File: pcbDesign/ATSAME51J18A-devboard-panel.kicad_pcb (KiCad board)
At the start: 2 copper layers, 100 x 100 mm, 300 parts, among them J1 Micro_SD_Card, J10 CAN, J2 BAT, J3 QWIIC, J4 L_PINS, J5 NP_OUT, J6 USB, J7 QSPI, J8 R_PINS, J9 USB4105_REVA, U1 TCAN1051GVDRQ1, U2 ATSAME51J18A-A, U3 MIC5219-5.0YMM, U4 LM27762, U5 LM2775QDSGTQ1, U6 SC630AULTRT, U7 BQ24074RGT, U8 BQ27441DRZR-G1B, Y1 32.768

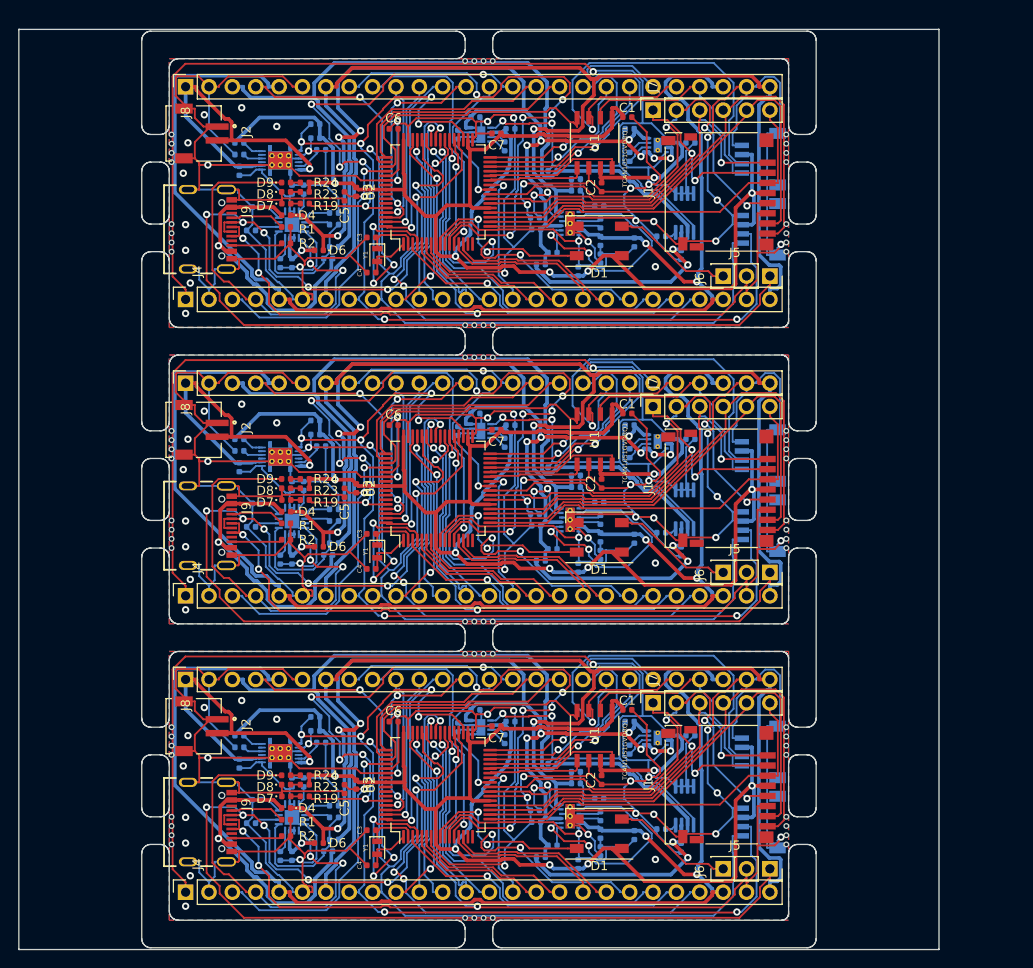
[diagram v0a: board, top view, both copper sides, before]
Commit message: Repanelized board after adding pin descriptions
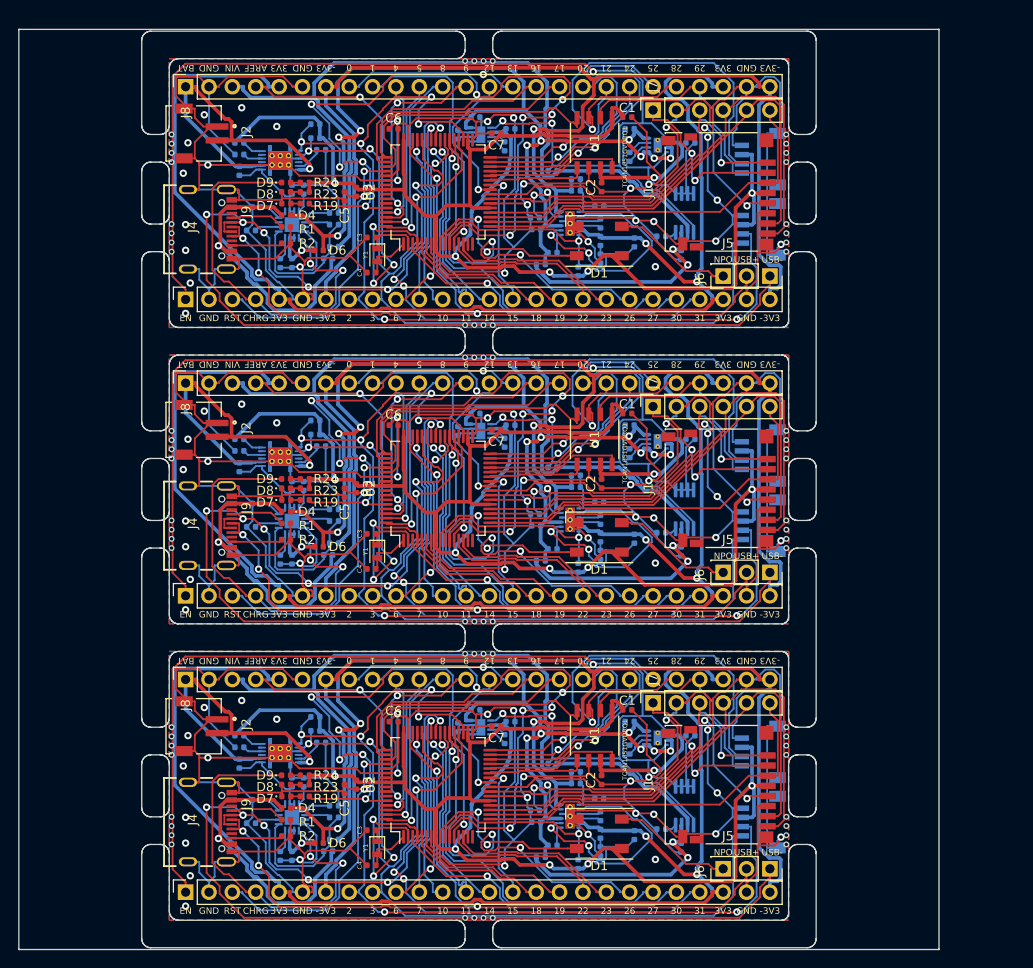
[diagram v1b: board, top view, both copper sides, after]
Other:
- board text added: "-3V3"
- board text added: "-3v3"
- board text added: "0"
- board text added: "1"
- board text added: "10"
- board text added: "11"
- board text added: "12"
- board text added: "13"
- board text added: "14"
- board text added: "15"
- board text added: "16"
- board text added: "17"
- board text added: "18"
- board text added: "19"
- board text added: "2"
- board text added: "20"
- board text added: "21"
- board text added: "22"
- board text added: "23"
- board text added: "24"
- board text added: "25"
- board text added: "26"
- board text added: "27"
- board text added: "28"
- board text added: "29"
- board text added: "3"
- board text added: "30"
- board text added: "31"
- board text added: "3V3"
- board text added: "4"
- board text added: "5"
- board text added: "6"
- board text added: "7"
- board text added: "8"
- board text added: "9"
- board text added: "AREF"
- board text added: "BAT"
- board text added: "CANH"
- board text added: "CANL"
- board text added: "CHRG"
- board text added: "CS"
- board text added: "EN"
- board text added: "GND"
- board text added: "I2SDI"
- board text added: "I2SDO"
- board text added: "I2SMCLK"
- board text added: "I2SSCK"
- board text added: "I2SWS"
- board text added: "MI"
- board text added: "MO"
- board text added: "NPO"
- board text added: "QCS"
- board text added: "QD0"
- board text added: "QD1"
- board text added: "QD2"
- board text added: "QD3"
- board text added: "QSCK"
- board text added: "RST"
- board text added: "RX"
- board text added: "SCK"
- board text added: "SCL"
- board text added: "SDA"
- board text added: "TX"
- board text added: "USB+"
- board text added: "USB-"
- board text added: "VIN"

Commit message: Panelized the final design
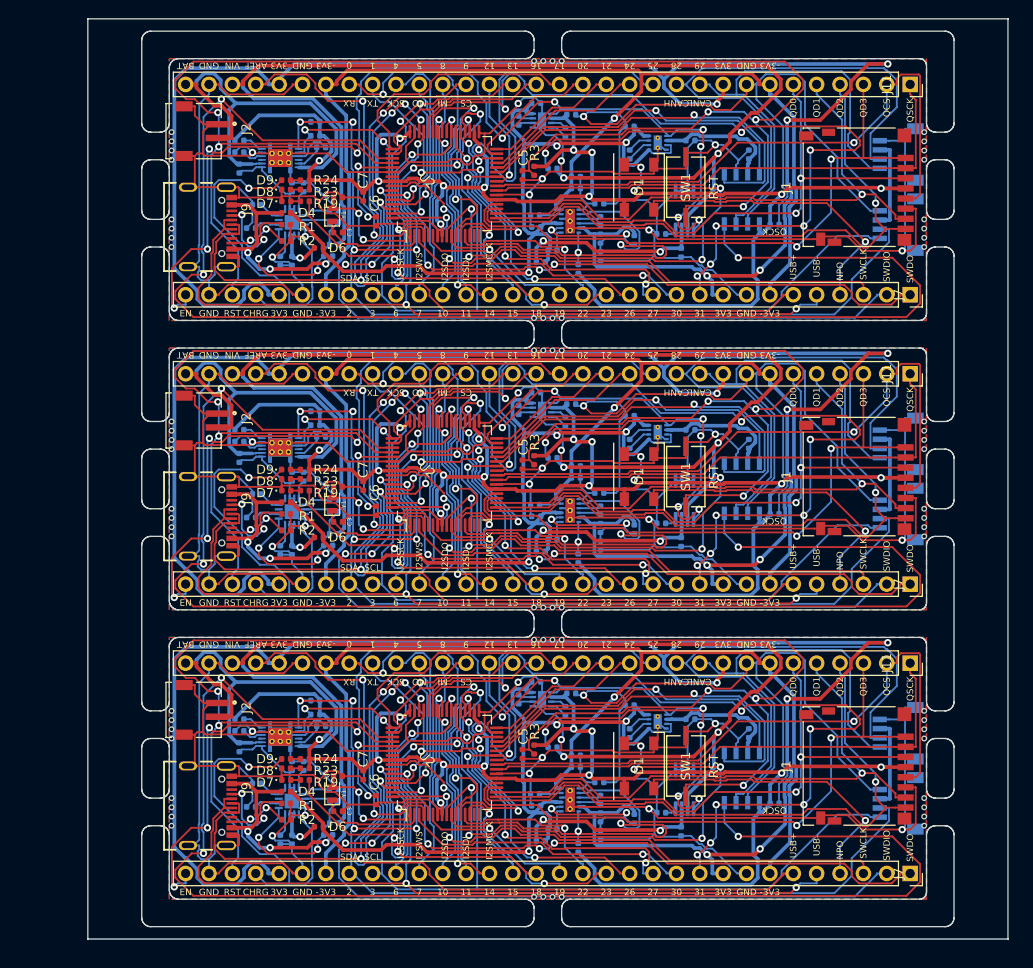
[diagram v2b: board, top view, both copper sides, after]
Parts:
- removed the C1 at (99.8, 120.8)
- removed the C1 at (99.8, 88.6)
- removed the C1 at (99.8, 56.4)
- removed the C10 at (100.0, 122.0)
- removed the C10 at (100.0, 89.8)
- removed the C10 at (100.0, 57.6)
- removed the C11 at (89.9, 133.0)
- removed the C11 at (89.9, 100.8)
- removed the C11 at (89.9, 68.5)
- removed the C12 at (105.6, 135.8)
- removed the C12 at (105.6, 103.5)
- removed the C12 at (105.6, 71.3)
- removed the C13 at (89.8, 131.7)
- removed the C13 at (89.8, 99.5)
- removed the C13 at (89.8, 67.3)
- removed the C14 at (100.0, 125.1)
- removed the C14 at (100.0, 92.9)
- removed the C14 at (100.0, 60.7)
- removed the C15 at (100.5, 134.4)
- removed the C15 at (100.5, 102.2)
- removed the C15 at (100.5, 70.0)
- removed the C16 at (94.2, 127.5)
- removed the C16 at (94.2, 95.3)
- removed the C16 at (94.2, 63.1)
- removed the C17 at (86.4, 123.9)
- removed the C17 at (86.4, 91.7)
- removed the C17 at (86.4, 59.5)
- removed the C18 at (106.6, 123.6)
- removed the C18 at (106.6, 91.4)
- removed the C18 at (106.6, 59.1)
- removed the C19 at (87.1, 122.0)
- removed the C19 at (87.1, 89.8)
- removed the C19 at (87.1, 57.6)
- removed the C2 at (97.0, 128.4)
- removed the C2 at (97.0, 96.2)
- removed the C2 at (97.0, 64.0)
- removed the C20 at (83.3, 120.8)
- removed the C20 at (83.3, 88.6)
- removed the C20 at (83.3, 56.4)
- removed the C21 at (81.4, 122.7)
- removed the C21 at (81.4, 90.5)
- removed the C21 at (81.4, 58.3)
- removed the C22 at (63.3, 136.6)
- removed the C22 at (63.3, 104.4)
- removed the C22 at (63.3, 72.2)
- removed the C23 at (63.3, 128.6)
- removed the C23 at (63.3, 96.4)
- removed the C23 at (63.3, 64.2)
- removed the C24 at (66.5, 124.3)
- removed the C24 at (66.5, 92.1)
- removed the C24 at (66.5, 59.9)
- removed the C3 at (72.0, 133.9)
- removed the C3 at (72.0, 101.6)
- removed the C3 at (72.0, 69.4)
- removed the C4 at (72.0, 137.7)
- removed the C4 at (72.0, 105.5)
- removed the C4 at (72.0, 73.2)
- removed the C5 at (69.1, 129.4)
- removed the C5 at (69.1, 97.2)
- removed the C5 at (69.1, 65.0)
- removed the C6 at (74.4, 122.0)
- removed the C6 at (74.4, 89.8)
- removed the C6 at (74.4, 57.6)
- removed the C7 at (85.6, 122.5)
- removed the C7 at (85.6, 90.3)
- removed the C7 at (85.6, 58.1)
- removed the C8 at (103.5, 133.7)
- removed the C8 at (103.5, 101.5)
- removed the C8 at (103.5, 69.3)
- removed the C9 at (96.9, 132.3)
- removed the C9 at (96.9, 100.1)
- removed the C9 at (96.9, 67.9)
- removed the D1 at (96.7, 134.2)
- removed the D1 at (96.7, 102.0)
- removed the D1 at (96.7, 69.8)
- removed the D2 at (67.3, 136.1)
- removed the D2 at (67.3, 103.9)
- removed the D2 at (67.3, 71.7)
- removed the D3 at (67.9, 134.9)
- removed the D3 at (67.9, 102.7)
- removed the D3 at (67.9, 70.4)
- removed the D4 at (62.7, 131.4)
- removed the D4 at (62.7, 99.2)
- removed the D4 at (62.7, 67.0)
- removed the D5 at (90.4, 136.8)
- removed the D5 at (90.4, 104.6)
- removed the D5 at (90.4, 72.4)
- removed the D6 at (66.3, 135.2)
- removed the D6 at (66.3, 103.0)
- removed the D6 at (66.3, 70.8)
- removed the D7 at (62.7, 130.2)
- removed the D7 at (62.7, 98.0)
- removed the D7 at (62.7, 65.7)
- removed the D8 at (62.7, 128.9)
- removed the D8 at (62.7, 96.7)
- removed the D8 at (62.7, 64.5)
- removed the D9 at (62.7, 127.9)
- removed the D9 at (62.7, 95.7)
- removed the D9 at (62.7, 63.5)
- removed the J1 at (109.7, 128.9)
- removed the J1 at (109.7, 96.7)
- removed the J1 at (109.7, 64.5)
- removed the J10 at (112.2, 125.3)
- removed the J10 at (112.2, 93.1)
- removed the J10 at (112.2, 60.9)
- removed the J2 at (53.0, 122.5)
- removed the J2 at (53.0, 90.3)
- removed the J2 at (53.0, 58.1)
- removed the J3 at (112.2, 133.0)
- removed the J3 at (112.2, 100.8)
- removed the J3 at (112.2, 68.5)
- removed J4 (x3): L_PINS, Connector_PinSocket_2.54mm:PinSocket_1x26_P2.54mm_Vertical
- removed J5 (x3): NP_OUT, Connector_PinSocket_2.54mm:PinSocket_1x01_P2.54mm_Vertical
- removed J6 (x3): USB, Connector_PinSocket_2.54mm:PinSocket_1x02_P2.54mm_Vertical
- removed the J7 at (102.6, 120.0)
- removed the J7 at (102.6, 87.8)
- removed the J7 at (102.6, 55.6)
- removed J8 (x3): R_PINS, Connector_PinSocket_2.54mm:PinSocket_1x26_P2.54mm_Vertical
- removed the J9 at (52.0, 133.0)
- removed the J9 at (52.0, 100.8)
- removed the J9 at (52.0, 68.5)
- removed the R1 at (62.7, 132.7)
- removed the R1 at (62.7, 100.5)
- removed the R1 at (62.7, 68.3)
- removed the R10 at (96.7, 130.4)
- removed the R10 at (96.7, 98.2)
- removed the R10 at (96.7, 66.0)
- removed the R11 at (58.9, 133.1)
- removed the R11 at (58.9, 100.9)
- removed the R11 at (58.9, 68.7)
- removed the R12 at (62.1, 136.6)
- removed the R12 at (62.1, 104.4)
- removed the R12 at (62.1, 72.2)
- removed the R13 at (59.5, 130.5)
- removed the R13 at (59.5, 98.3)
- removed the R13 at (59.5, 66.1)
- removed the R14 at (65.9, 121.5)
- removed the R14 at (65.9, 89.3)
- removed the R14 at (65.9, 57.1)
- removed the R15 at (65.9, 123.1)
- removed the R15 at (65.9, 90.8)
- removed the R15 at (65.9, 58.6)
- removed the R16 at (57.6, 126.6)
- removed the R16 at (57.6, 94.4)
- removed the R16 at (57.6, 62.2)
- removed the R17 at (57.6, 124.8)
- removed the R17 at (57.6, 92.6)
- removed the R17 at (57.6, 60.4)
- removed the R18 at (57.6, 123.6)
- removed the R18 at (57.6, 91.4)
- removed the R18 at (57.6, 59.1)
- removed the R19 at (64.7, 130.2)
- removed the R19 at (64.7, 98.0)
- removed the R19 at (64.7, 65.7)
- removed the R2 at (62.7, 134.5)
- removed the R2 at (62.7, 102.3)
- removed the R2 at (62.7, 70.1)
- removed the R20 at (67.9, 132.5)
- removed the R20 at (67.9, 100.2)
- removed the R20 at (67.9, 68.0)
- removed the R21 at (67.9, 131.2)
- removed the R21 at (67.9, 99.0)
- removed the R21 at (67.9, 66.8)
- removed the R22 at (64.6, 128.6)
- removed the R22 at (64.6, 96.4)
- removed the R22 at (64.6, 64.2)
- removed the R23 at (64.7, 128.9)
- removed the R23 at (64.7, 96.7)
- removed the R23 at (64.7, 64.5)
- removed the R24 at (64.7, 127.9)
- removed the R24 at (64.7, 95.7)
- removed the R24 at (64.7, 63.5)
- removed the R3 at (70.3, 128.9)
- removed the R3 at (70.3, 96.7)
- removed the R3 at (70.3, 64.5)
- removed the R4 at (91.7, 126.6)
- removed the R4 at (91.7, 94.4)
- removed the R4 at (91.7, 62.2)
- removed the R5 at (94.5, 137.5)
- removed the R5 at (94.5, 105.3)
- removed the R5 at (94.5, 73.1)
- removed the R6 at (91.7, 135.5)
- removed the R6 at (91.7, 103.3)
- removed the R6 at (91.7, 71.1)
- removed the R7 at (96.9, 134.2)
- removed the R7 at (96.9, 102.0)
- removed the R7 at (96.9, 69.8)
- removed the R8 at (94.2, 128.8)
- removed the R8 at (94.2, 96.6)
- removed the R8 at (94.2, 64.4)
- removed the R9 at (96.9, 136.1)
- removed the R9 at (96.9, 103.9)
- removed the R9 at (96.9, 71.7)
- removed the REF** at (117.1, 135.4)
- removed the REF** at (50.2, 133.4)
- removed the REF** at (50.2, 134.4)
- removed the REF** at (50.2, 135.4)
- removed the REF** at (50.2, 122.7)
- removed the REF** at (50.2, 123.7)
- removed the REF** at (50.2, 124.7)
- removed the REF** at (50.2, 125.7)
- removed the REF** at (117.1, 103.2)
- removed the REF** at (117.1, 102.2)
- removed the REF** at (117.1, 101.2)
- removed the REF** at (117.1, 134.4)
- removed the REF** at (117.1, 100.2)
- removed the REF** at (117.1, 93.4)
- removed the REF** at (117.1, 92.4)
- removed the REF** at (117.1, 91.4)
- removed the REF** at (117.1, 90.4)
- removed the REF** at (50.2, 100.2)
- removed the REF** at (50.2, 101.2)
- removed the REF** at (50.2, 102.2)
- removed the REF** at (50.2, 103.2)
- removed the REF** at (50.2, 90.4)
- removed the REF** at (117.1, 133.4)
- removed the REF** at (50.2, 91.4)
- removed the REF** at (50.2, 92.4)
- removed the REF** at (50.2, 93.4)
- removed the REF** at (117.1, 71.0)
- removed the REF** at (117.1, 70.0)
- removed the REF** at (117.1, 69.0)
- removed the REF** at (117.1, 68.0)
- removed the REF** at (117.1, 61.2)
- removed the REF** at (117.1, 60.2)
- removed the REF** at (117.1, 59.2)
- removed the REF** at (117.1, 132.4)
- removed the REF** at (117.1, 58.2)
- removed the REF** at (50.2, 68.0)
- removed the REF** at (50.2, 69.0)
- removed the REF** at (50.2, 70.0)
- removed the REF** at (50.2, 71.0)
- removed the REF** at (50.2, 58.2)
- removed the REF** at (50.2, 59.2)
- removed the REF** at (50.2, 60.2)
- removed the REF** at (50.2, 61.2)
- removed the REF** at (82.2, 143.4)
- removed the REF** at (117.1, 125.7)
- removed the REF** at (83.2, 143.4)
- removed the REF** at (84.2, 143.4)
- removed the REF** at (85.2, 143.4)
- removed the REF** at (85.2, 114.7)
- removed the REF** at (84.2, 114.7)
- removed the REF** at (83.2, 114.7)
- removed the REF** at (82.2, 114.7)
- removed the REF** at (82.2, 111.2)
- removed the REF** at (83.2, 111.2)
- removed the REF** at (84.2, 111.2)
- removed the REF** at (117.1, 124.7)
- removed the REF** at (85.2, 111.2)
- removed the REF** at (85.2, 82.5)
- removed the REF** at (84.2, 82.5)
- removed the REF** at (83.2, 82.5)
- removed the REF** at (82.2, 82.5)
- removed the REF** at (82.2, 79.0)
- removed the REF** at (83.2, 79.0)
- removed the REF** at (84.2, 79.0)
- removed the REF** at (85.2, 79.0)
- removed the REF** at (85.2, 50.2)
- removed the REF** at (117.1, 123.7)
- removed the REF** at (84.2, 50.2)
- removed the REF** at (83.2, 50.2)
- removed the REF** at (82.2, 50.2)
- removed the REF** at (117.1, 122.7)
- removed the REF** at (50.2, 132.4)
- removed the U1 at (96.2, 123.6)
- removed the U1 at (96.2, 91.4)
- removed the U1 at (96.2, 59.1)
- removed the U2 at (79.2, 128.9)
- removed the U2 at (79.2, 96.7)
- removed the U2 at (79.2, 64.5)
- removed the U3 at (106.0, 131.2)
- removed the U3 at (106.0, 99.0)
- removed the U3 at (106.0, 66.8)
- removed the U4 at (93.6, 132.3)
- removed the U4 at (93.6, 100.1)
- removed the U4 at (93.6, 67.9)
- removed the U5 at (103.1, 123.8)
- removed the U5 at (103.1, 91.6)
- removed the U5 at (103.1, 59.4)
- removed the U6 at (83.9, 122.7)
- removed the U6 at (83.9, 90.5)
- removed the U6 at (83.9, 58.3)
- removed the U7 at (63.3, 132.5)
- removed the U7 at (63.3, 100.2)
- removed the U7 at (63.3, 68.0)
- removed the U8 at (62.1, 125.5)
- removed the U8 at (62.1, 93.3)
- removed the U8 at (62.1, 61.0)
- removed the Y1 at (72.6, 135.8)
- removed the Y1 at (72.6, 103.5)
- removed the Y1 at (72.6, 71.3)
- added C1: 100n, Capacitor_SMD:C_0402_1005Metric, B.Cu at (115.8, 130.9)
- added C1: 100n, Capacitor_SMD:C_0402_1005Metric, B.Cu at (115.8, 99.5)
- added C1: 100n, Capacitor_SMD:C_0402_1005Metric, B.Cu at (115.8, 68.0)
- added C10: 10u, Capacitor_SMD:C_0402_1005Metric, B.Cu at (100.0, 120.3)
- added C10: 10u, Capacitor_SMD:C_0402_1005Metric, B.Cu at (100.0, 88.8)
- added C10: 10u, Capacitor_SMD:C_0402_1005Metric, B.Cu at (100.0, 57.4)
- added C11: 4.7u, Capacitor_SMD:C_0402_1005Metric, B.Cu at (89.9, 131.2)
- added C11: 4.7u, Capacitor_SMD:C_0402_1005Metric, B.Cu at (89.9, 99.7)
- added C11: 4.7u, Capacitor_SMD:C_0402_1005Metric, B.Cu at (89.9, 68.3)
- added C12: 2.2u, Capacitor_SMD:C_0402_1005Metric, B.Cu at (105.6, 134.0)
- added C12: 2.2u, Capacitor_SMD:C_0402_1005Metric, B.Cu at (105.6, 102.5)
- added C12: 2.2u, Capacitor_SMD:C_0402_1005Metric, B.Cu at (105.6, 71.1)
- added C13: 4.7u, Capacitor_SMD:C_0402_1005Metric, B.Cu at (89.8, 129.9)
- added C13: 4.7u, Capacitor_SMD:C_0402_1005Metric, B.Cu at (89.8, 98.5)
- added C13: 4.7u, Capacitor_SMD:C_0402_1005Metric, B.Cu at (89.8, 67.0)
- added C14: 1u, Capacitor_SMD:C_0402_1005Metric, B.Cu at (100.0, 123.3)
- added C14: 1u, Capacitor_SMD:C_0402_1005Metric, B.Cu at (100.0, 91.9)
- added C14: 1u, Capacitor_SMD:C_0402_1005Metric, B.Cu at (100.0, 60.4)
- added C15: 2.2u, Capacitor_SMD:C_0402_1005Metric, B.Cu at (100.5, 132.6)
- added C15: 2.2u, Capacitor_SMD:C_0402_1005Metric, B.Cu at (100.5, 101.2)
- added C15: 2.2u, Capacitor_SMD:C_0402_1005Metric, B.Cu at (100.5, 69.7)
- added C16: 2.2u, Capacitor_SMD:C_0402_1005Metric, B.Cu at (94.2, 125.7)
- added C16: 2.2u, Capacitor_SMD:C_0402_1005Metric, B.Cu at (94.2, 94.3)
- added C16: 2.2u, Capacitor_SMD:C_0402_1005Metric, B.Cu at (94.2, 62.8)
- added C17: 2.2u, Capacitor_SMD:C_0402_1005Metric, B.Cu at (93.1, 120.9)
- added C17: 2.2u, Capacitor_SMD:C_0402_1005Metric, B.Cu at (93.1, 89.4)
- added C17: 2.2u, Capacitor_SMD:C_0402_1005Metric, B.Cu at (93.1, 58.0)
- added C18: 10u, Capacitor_SMD:C_0402_1005Metric, B.Cu at (106.6, 121.8)
- added C18: 10u, Capacitor_SMD:C_0402_1005Metric, B.Cu at (106.6, 90.3)
- added C18: 10u, Capacitor_SMD:C_0402_1005Metric, B.Cu at (106.6, 58.9)
- added C19: 4.7u, Capacitor_SMD:C_0402_1005Metric, B.Cu at (93.7, 119.0)
- added C19: 4.7u, Capacitor_SMD:C_0402_1005Metric, B.Cu at (93.7, 87.5)
- added C19: 4.7u, Capacitor_SMD:C_0402_1005Metric, B.Cu at (93.7, 56.1)
- added C2: 100n, Capacitor_SMD:C_0402_1005Metric, B.Cu at (113.0, 123.3)
- added C2: 100n, Capacitor_SMD:C_0402_1005Metric, B.Cu at (113.0, 91.9)
- added C2: 100n, Capacitor_SMD:C_0402_1005Metric, B.Cu at (113.0, 60.4)
- added C20: 4.7u, Capacitor_SMD:C_0402_1005Metric, B.Cu at (89.9, 117.7)
- added C20: 4.7u, Capacitor_SMD:C_0402_1005Metric, B.Cu at (89.9, 86.3)
- added C20: 4.7u, Capacitor_SMD:C_0402_1005Metric, B.Cu at (89.9, 54.8)
- added C21: 2.2u, Capacitor_SMD:C_0402_1005Metric, B.Cu at (88.0, 119.6)
- added C21: 2.2u, Capacitor_SMD:C_0402_1005Metric, B.Cu at (88.0, 88.2)
- added C21: 2.2u, Capacitor_SMD:C_0402_1005Metric, B.Cu at (88.0, 56.7)
- added C22: 4.7u, Capacitor_SMD:C_0402_1005Metric, B.Cu at (63.3, 134.9)
- added C22: 4.7u, Capacitor_SMD:C_0402_1005Metric, B.Cu at (63.3, 103.4)
- added C22: 4.7u, Capacitor_SMD:C_0402_1005Metric, B.Cu at (63.3, 72.0)
- added C23: 4.7u, Capacitor_SMD:C_0402_1005Metric, B.Cu at (63.3, 126.9)
- added C23: 4.7u, Capacitor_SMD:C_0402_1005Metric, B.Cu at (63.3, 95.4)
- added C23: 4.7u, Capacitor_SMD:C_0402_1005Metric, B.Cu at (63.3, 64.0)
- added C24: 0.47u, Capacitor_SMD:C_0402_1005Metric, B.Cu at (66.5, 122.5)
- added C24: 0.47u, Capacitor_SMD:C_0402_1005Metric, B.Cu at (66.5, 91.1)
- added C24: 0.47u, Capacitor_SMD:C_0402_1005Metric, B.Cu at (66.5, 59.7)
- added C3: 22u, Capacitor_SMD:C_0402_1005Metric, F.Cu at (68.3, 131.8)
- added C3: 22u, Capacitor_SMD:C_0402_1005Metric, F.Cu at (68.3, 100.3)
- added C3: 22u, Capacitor_SMD:C_0402_1005Metric, F.Cu at (68.3, 68.9)
- added C4: 22u, Capacitor_SMD:C_0402_1005Metric, F.Cu at (68.3, 128.0)
- added C4: 22u, Capacitor_SMD:C_0402_1005Metric, F.Cu at (68.3, 96.5)
- added C4: 22u, Capacitor_SMD:C_0402_1005Metric, F.Cu at (68.3, 65.1)
- added C5: 1u, Capacitor_SMD:C_0402_1005Metric, F.Cu at (88.4, 125.6)
- added C5: 1u, Capacitor_SMD:C_0402_1005Metric, F.Cu at (88.4, 94.1)
- added C5: 1u, Capacitor_SMD:C_0402_1005Metric, F.Cu at (88.4, 62.7)
- added C6: 1u, Capacitor_SMD:C_0402_1005Metric, F.Cu at (72.5, 130.6)
- added C6: 1u, Capacitor_SMD:C_0402_1005Metric, F.Cu at (72.5, 99.1)
- added C6: 1u, Capacitor_SMD:C_0402_1005Metric, F.Cu at (72.5, 67.7)
- added C7: 500n, Capacitor_SMD:C_0402_1005Metric, F.Cu at (71.1, 127.9)
- added C7: 500n, Capacitor_SMD:C_0402_1005Metric, F.Cu at (71.1, 96.4)
- added C7: 500n, Capacitor_SMD:C_0402_1005Metric, F.Cu at (71.1, 65.0)
- added C8: 0.47u, Capacitor_SMD:C_0402_1005Metric, B.Cu at (103.5, 131.9)
- added C8: 0.47u, Capacitor_SMD:C_0402_1005Metric, B.Cu at (103.5, 100.5)
- added C8: 0.47u, Capacitor_SMD:C_0402_1005Metric, B.Cu at (103.5, 69.1)
- added C9: 0.47u, Capacitor_SMD:C_0402_1005Metric, B.Cu at (96.9, 130.5)
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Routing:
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- added copper zone on F.Cu, net (none)
- removed copper zone on F.Cu, net Board_1-GND
- removed copper zone on F.Cu, net Board_2-GND
- removed copper zone on F.Cu, net Board_3-GND
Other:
- outline, holes or cut-outs redrawn
- board text added: "SWCLK"
- board text added: "SWDIO"
- board text added: "SWDO"

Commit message: Panelized the prototype(v0.1)
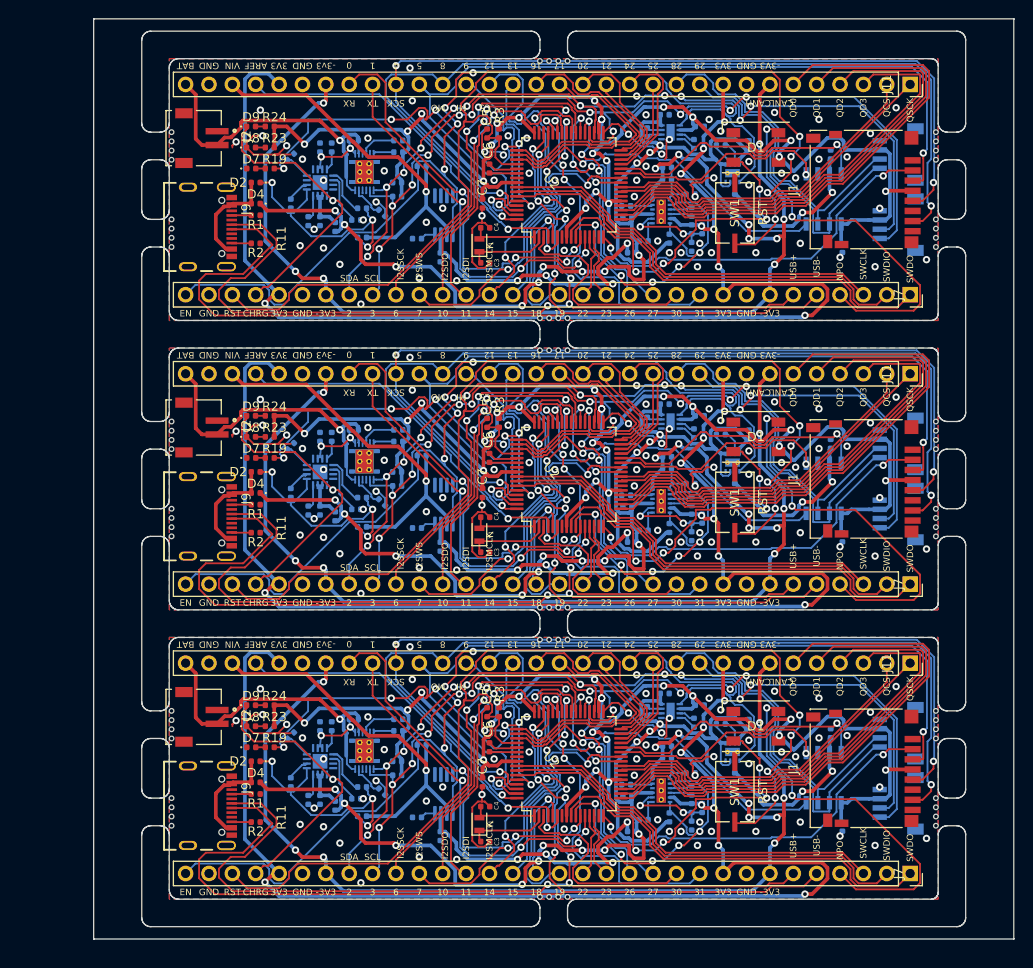
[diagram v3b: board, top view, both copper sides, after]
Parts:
- removed the C1 at (115.8, 130.9)
- removed the C1 at (115.8, 99.5)
- removed the C1 at (115.8, 68.0)
- removed the C10 at (100.0, 120.3)
- removed the C10 at (100.0, 88.8)
- removed the C10 at (100.0, 57.4)
- removed the C11 at (89.9, 131.2)
- removed the C11 at (89.9, 99.7)
- removed the C11 at (89.9, 68.3)
- removed the C12 at (105.6, 134.0)
- removed the C12 at (105.6, 102.5)
- removed the C12 at (105.6, 71.1)
- removed the C13 at (89.8, 129.9)
- removed the C13 at (89.8, 98.5)
- removed the C13 at (89.8, 67.0)
- removed the C14 at (100.0, 123.3)
- removed the C14 at (100.0, 91.9)
- removed the C14 at (100.0, 60.4)
- removed the C15 at (100.5, 132.6)
- removed the C15 at (100.5, 101.2)
- removed the C15 at (100.5, 69.7)
- removed the C16 at (94.2, 125.7)
- removed the C16 at (94.2, 94.3)
- removed the C16 at (94.2, 62.8)
- removed the C17 at (93.1, 120.9)
- removed the C17 at (93.1, 89.4)
- removed the C17 at (93.1, 58.0)
- removed the C18 at (106.6, 121.8)
- removed the C18 at (106.6, 90.3)
- removed the C18 at (106.6, 58.9)
- removed the C19 at (93.7, 119.0)
- removed the C19 at (93.7, 87.5)
- removed the C19 at (93.7, 56.1)
- removed the C2 at (113.0, 123.3)
- removed the C2 at (113.0, 91.9)
- removed the C2 at (113.0, 60.4)
- removed the C20 at (89.9, 117.7)
- removed the C20 at (89.9, 86.3)
- removed the C20 at (89.9, 54.8)
- removed the C21 at (88.0, 119.6)
- removed the C21 at (88.0, 88.2)
- removed the C21 at (88.0, 56.7)
- removed the C22 at (63.3, 134.9)
- removed the C22 at (63.3, 103.4)
- removed the C22 at (63.3, 72.0)
- removed the C23 at (63.3, 126.9)
- removed the C23 at (63.3, 95.4)
- removed the C23 at (63.3, 64.0)
- removed the C24 at (66.5, 122.5)
- removed the C24 at (66.5, 91.1)
- removed the C24 at (66.5, 59.7)
- removed the C3 at (68.3, 131.8)
- removed the C3 at (68.3, 100.3)
- removed the C3 at (68.3, 68.9)
- removed the C4 at (68.3, 128.0)
- removed the C4 at (68.3, 96.5)
- removed the C4 at (68.3, 65.1)
- removed the C5 at (88.4, 125.6)
- removed the C5 at (88.4, 94.1)
- removed the C5 at (88.4, 62.7)
- removed the C6 at (72.5, 130.6)
- removed the C6 at (72.5, 99.1)
- removed the C6 at (72.5, 67.7)
- removed the C7 at (71.1, 127.9)
- removed the C7 at (71.1, 96.4)
- removed the C7 at (71.1, 65.0)
- removed the C8 at (103.5, 131.9)
- removed the C8 at (103.5, 100.5)
- removed the C8 at (103.5, 69.1)
- removed the C9 at (96.9, 130.5)
- removed the C9 at (96.9, 99.1)
- removed the C9 at (96.9, 67.7)
- removed the D1 at (101.1, 126.9)
- removed the D1 at (101.1, 95.4)
- removed the D1 at (101.1, 64.0)
- removed the D2 at (67.3, 134.4)
- removed the D2 at (67.3, 102.9)
- removed the D2 at (67.3, 71.5)
- removed the D3 at (67.9, 133.1)
- removed the D3 at (67.9, 101.6)
- removed the D3 at (67.9, 70.2)
- removed the D4 at (62.7, 129.7)
- removed the D4 at (62.7, 98.2)
- removed the D4 at (62.7, 66.8)
- removed the D5 at (90.4, 135.0)
- removed the D5 at (90.4, 103.5)
- removed the D5 at (90.4, 72.1)
- removed the D6 at (66.3, 133.5)
- removed the D6 at (66.3, 102.0)
- removed the D6 at (66.3, 70.6)
- removed the D7 at (62.7, 128.4)
- removed the D7 at (62.7, 96.9)
- removed the D7 at (62.7, 65.5)
- removed the D8 at (62.7, 127.1)
- removed the D8 at (62.7, 95.7)
- removed the D8 at (62.7, 64.2)
- removed the D9 at (62.7, 126.1)
- removed the D9 at (62.7, 94.7)
- removed the D9 at (62.7, 63.2)
- removed the J1 at (124.7, 126.9)
- removed the J1 at (124.7, 95.4)
- removed the J1 at (124.7, 64.0)
- removed the J2 at (53.0, 120.8)
- removed the J2 at (53.0, 89.3)
- removed the J2 at (53.0, 57.9)
- removed the R1 at (62.7, 130.9)
- removed the R1 at (62.7, 99.5)
- removed the R1 at (62.7, 68.0)
- removed the R10 at (96.7, 128.6)
- removed the R10 at (96.7, 97.2)
- removed the R10 at (96.7, 65.7)
- removed the R11 at (58.9, 131.3)
- removed the R11 at (58.9, 99.9)
- removed the R11 at (58.9, 68.4)
- removed the R12 at (62.1, 134.9)
- removed the R12 at (62.1, 103.4)
- removed the R12 at (62.1, 72.0)
- removed the R13 at (59.5, 128.8)
- removed the R13 at (59.5, 97.3)
- removed the R13 at (59.5, 65.9)
- removed the R14 at (65.9, 119.8)
- removed the R14 at (65.9, 88.3)
- removed the R14 at (65.9, 56.9)
- removed the R15 at (65.9, 121.3)
- removed the R15 at (65.9, 89.8)
- removed the R15 at (65.9, 58.4)
- removed the R16 at (57.6, 124.8)
- removed the R16 at (57.6, 93.4)
- removed the R16 at (57.6, 61.9)
- removed the R17 at (57.6, 123.1)
- removed the R17 at (57.6, 91.6)
- removed the R17 at (57.6, 60.2)
- removed the R18 at (57.6, 121.8)
- removed the R18 at (57.6, 90.3)
- removed the R18 at (57.6, 58.9)
- removed the R19 at (64.7, 128.4)
- removed the R19 at (64.7, 96.9)
- removed the R19 at (64.7, 65.5)
- removed the R2 at (62.7, 132.7)
- removed the R2 at (62.7, 101.3)
- removed the R2 at (62.7, 69.8)
- removed the R20 at (67.9, 130.7)
- removed the R20 at (67.9, 99.2)
- removed the R20 at (67.9, 67.8)
- removed the R21 at (67.9, 129.4)
- removed the R21 at (67.9, 98.0)
- removed the R21 at (67.9, 66.5)
- removed the R22 at (64.6, 126.9)
- removed the R22 at (64.6, 95.4)
- removed the R22 at (64.6, 64.0)
- removed the R23 at (64.7, 127.1)
- removed the R23 at (64.7, 95.7)
- removed the R23 at (64.7, 64.2)
- removed the R24 at (64.7, 126.1)
- removed the R24 at (64.7, 94.7)
- removed the R24 at (64.7, 63.2)
- removed the R3 at (89.7, 125.1)
- removed the R3 at (89.7, 93.6)
- removed the R3 at (89.7, 62.2)
- removed the R4 at (91.7, 124.8)
- removed the R4 at (91.7, 93.4)
- removed the R4 at (91.7, 61.9)
- removed the R5 at (94.5, 135.8)
- removed the R5 at (94.5, 104.3)
- removed the R5 at (94.5, 72.9)
- removed the R6 at (91.7, 133.7)
- removed the R6 at (91.7, 102.3)
- removed the R6 at (91.7, 70.8)
- removed the R7 at (96.9, 132.5)
- removed the R7 at (96.9, 101.0)
- removed the R7 at (96.9, 69.6)
- removed the R8 at (94.2, 127.0)
- removed the R8 at (94.2, 95.5)
- removed the R8 at (94.2, 64.1)
- removed the R9 at (96.9, 134.4)
- removed the R9 at (96.9, 102.9)
- removed the R9 at (96.9, 71.5)
- removed the REF** at (132.0, 133.4)
- removed the REF** at (132.0, 101.9)
- removed the REF** at (132.0, 100.9)
- removed the REF** at (132.0, 99.9)
- removed the REF** at (132.0, 132.4)
- removed the REF** at (132.0, 98.9)
- removed the REF** at (132.0, 92.4)
- removed the REF** at (132.0, 91.4)
- removed the REF** at (132.0, 90.4)
- removed the REF** at (132.0, 89.4)
- removed the REF** at (132.0, 131.4)
- removed the REF** at (132.0, 70.5)
- removed the REF** at (132.0, 69.5)
- removed the REF** at (132.0, 68.5)
- removed the REF** at (132.0, 67.5)
- removed the REF** at (132.0, 61.0)
- removed the REF** at (132.0, 60.0)
- removed the REF** at (132.0, 59.0)
- removed the REF** at (132.0, 130.4)
- removed the REF** at (132.0, 58.0)
- removed the REF** at (89.6, 141.1)
- removed the REF** at (132.0, 123.9)
- removed the REF** at (90.6, 141.1)
- removed the REF** at (91.6, 141.1)
- removed the REF** at (92.6, 141.1)
- removed the REF** at (92.6, 113.1)
- removed the REF** at (91.6, 113.1)
- removed the REF** at (90.6, 113.1)
- removed the REF** at (89.6, 113.1)
- removed the REF** at (89.6, 109.6)
- removed the REF** at (90.6, 109.6)
- removed the REF** at (91.6, 109.6)
- removed the REF** at (132.0, 122.9)
- removed the REF** at (92.6, 109.6)
- removed the REF** at (92.6, 81.7)
- removed the REF** at (91.6, 81.7)
- removed the REF** at (90.6, 81.7)
- removed the REF** at (89.6, 81.7)
- removed the REF** at (89.6, 78.2)
- removed the REF** at (90.6, 78.2)
- removed the REF** at (91.6, 78.2)
- removed the REF** at (92.6, 78.2)
- removed the REF** at (92.6, 50.2)
- removed the REF** at (132.0, 121.9)
- removed the REF** at (91.6, 50.2)
- removed the REF** at (90.6, 50.2)
- removed the REF** at (89.6, 50.2)
- removed the REF** at (132.0, 120.9)
- removed the SW1 at (106.1, 126.9)
- removed the SW1 at (106.1, 95.4)
- removed the SW1 at (106.1, 64.0)
- removed the U1 at (112.2, 128.1)
- removed the U1 at (112.2, 96.7)
- removed the U1 at (112.2, 65.2)
- removed the U2 at (79.9, 126.5)
- removed the U2 at (79.9, 95.0)
- removed the U2 at (79.9, 63.6)
- removed the U3 at (106.0, 129.4)
- removed the U3 at (106.0, 98.0)
- removed the U3 at (106.0, 66.5)
- removed the U4 at (93.6, 130.5)
- removed the U4 at (93.6, 99.1)
- removed the U4 at (93.6, 67.7)
- removed the U5 at (103.1, 122.0)
- removed the U5 at (103.1, 90.6)
- removed the U5 at (103.1, 59.1)
- removed the U6 at (90.5, 119.6)
- removed the U6 at (90.5, 88.2)
- removed the U6 at (90.5, 56.7)
- removed the U7 at (63.3, 130.7)
- removed the U7 at (63.3, 99.2)
- removed the U7 at (63.3, 67.8)
- removed the U8 at (62.1, 123.7)
- removed the U8 at (62.1, 92.2)
- removed the U8 at (62.1, 60.8)
- removed the Y1 at (67.7, 129.9)
- removed the Y1 at (67.7, 98.4)
- removed the Y1 at (67.7, 67.0)
- added C1: 100n, Capacitor_SMD:C_0402_1005Metric, B.Cu at (123.2, 133.5)
- added C1: 100n, Capacitor_SMD:C_0402_1005Metric, B.Cu at (123.2, 102.0)
- added C1: 100n, Capacitor_SMD:C_0402_1005Metric, B.Cu at (123.2, 70.6)
- added C10: 10u, Capacitor_SMD:C_0402_1005Metric, B.Cu at (113.0, 122.3)
- added C10: 10u, Capacitor_SMD:C_0402_1005Metric, B.Cu at (113.0, 90.8)
- added C10: 10u, Capacitor_SMD:C_0402_1005Metric, B.Cu at (113.0, 59.4)
- added C11: 4.7u, Capacitor_SMD:C_0402_1005Metric, B.Cu at (99.8, 130.2)
- added C11: 4.7u, Capacitor_SMD:C_0402_1005Metric, B.Cu at (99.8, 98.7)
- added C11: 4.7u, Capacitor_SMD:C_0402_1005Metric, B.Cu at (99.8, 67.3)
- added C12: 2.2u, Capacitor_SMD:C_0402_1005Metric, B.Cu at (79.5, 134.5)
- added C12: 2.2u, Capacitor_SMD:C_0402_1005Metric, B.Cu at (79.5, 103.0)
- added C12: 2.2u, Capacitor_SMD:C_0402_1005Metric, B.Cu at (79.5, 71.6)
- added C13: 4.7u, Capacitor_SMD:C_0402_1005Metric, B.Cu at (99.7, 128.9)
- added C13: 4.7u, Capacitor_SMD:C_0402_1005Metric, B.Cu at (99.7, 97.5)
- added C13: 4.7u, Capacitor_SMD:C_0402_1005Metric, B.Cu at (99.7, 66.0)
- added C14: 1u, Capacitor_SMD:C_0402_1005Metric, B.Cu at (109.9, 122.3)
- added C14: 1u, Capacitor_SMD:C_0402_1005Metric, B.Cu at (109.9, 90.8)
- added C14: 1u, Capacitor_SMD:C_0402_1005Metric, B.Cu at (109.9, 59.4)
- added C15: 2.2u, Capacitor_SMD:C_0402_1005Metric, B.Cu at (107.9, 131.4)
- added C15: 2.2u, Capacitor_SMD:C_0402_1005Metric, B.Cu at (107.9, 100.0)
- added C15: 2.2u, Capacitor_SMD:C_0402_1005Metric, B.Cu at (107.9, 68.5)
- added C16: 2.2u, Capacitor_SMD:C_0402_1005Metric, B.Cu at (104.1, 124.7)
- added C16: 2.2u, Capacitor_SMD:C_0402_1005Metric, B.Cu at (104.1, 93.3)
- added C16: 2.2u, Capacitor_SMD:C_0402_1005Metric, B.Cu at (104.1, 61.8)
- added C17: 2.2u, Capacitor_SMD:C_0402_1005Metric, B.Cu at (107.0, 122.2)
- added C17: 2.2u, Capacitor_SMD:C_0402_1005Metric, B.Cu at (107.0, 90.7)
- added C17: 2.2u, Capacitor_SMD:C_0402_1005Metric, B.Cu at (107.0, 59.3)
- added C18: 10u, Capacitor_SMD:C_0402_1005Metric, B.Cu at (111.5, 128.1)
- added C18: 10u, Capacitor_SMD:C_0402_1005Metric, B.Cu at (111.5, 96.7)
- added C18: 10u, Capacitor_SMD:C_0402_1005Metric, B.Cu at (111.5, 65.2)
- added C19: 4.7u, Capacitor_SMD:C_0402_1005Metric, B.Cu at (107.7, 120.3)
- added C19: 4.7u, Capacitor_SMD:C_0402_1005Metric, B.Cu at (107.7, 88.8)
- added C19: 4.7u, Capacitor_SMD:C_0402_1005Metric, B.Cu at (107.7, 57.4)
- added C2: 100n, Capacitor_SMD:C_0402_1005Metric, B.Cu at (121.9, 123.3)
- added C2: 100n, Capacitor_SMD:C_0402_1005Metric, B.Cu at (121.9, 91.9)
- added C2: 100n, Capacitor_SMD:C_0402_1005Metric, B.Cu at (121.9, 60.4)
- added C20: 4.7u, Capacitor_SMD:C_0402_1005Metric, B.Cu at (103.8, 119.0)
- added C20: 4.7u, Capacitor_SMD:C_0402_1005Metric, B.Cu at (103.8, 87.5)
- added C20: 4.7u, Capacitor_SMD:C_0402_1005Metric, B.Cu at (103.8, 56.1)
- added C21: 2.2u, Capacitor_SMD:C_0402_1005Metric, B.Cu at (101.9, 120.9)
- added C21: 2.2u, Capacitor_SMD:C_0402_1005Metric, B.Cu at (101.9, 89.4)
- added C21: 2.2u, Capacitor_SMD:C_0402_1005Metric, B.Cu at (101.9, 58.0)
- added C22: 4.7u, Capacitor_SMD:C_0402_1005Metric, B.Cu at (66.4, 130.5)
- added C22: 4.7u, Capacitor_SMD:C_0402_1005Metric, B.Cu at (66.4, 99.1)
- added C22: 4.7u, Capacitor_SMD:C_0402_1005Metric, B.Cu at (66.4, 67.7)
- added C23: 4.7u, Capacitor_SMD:C_0402_1005Metric, B.Cu at (66.4, 122.5)
- added C23: 4.7u, Capacitor_SMD:C_0402_1005Metric, B.Cu at (66.4, 91.1)
- added C23: 4.7u, Capacitor_SMD:C_0402_1005Metric, B.Cu at (66.4, 59.7)
- added C24: 0.47u, Capacitor_SMD:C_0402_1005Metric, B.Cu at (73.1, 129.7)
- added C24: 0.47u, Capacitor_SMD:C_0402_1005Metric, B.Cu at (73.1, 98.2)
- added C24: 0.47u, Capacitor_SMD:C_0402_1005Metric, B.Cu at (73.1, 66.8)
- added C3: 22u, Capacitor_SMD:C_0402_1005Metric, F.Cu at (84.3, 135.1)
- added C3: 22u, Capacitor_SMD:C_0402_1005Metric, F.Cu at (84.3, 103.6)
- added C3: 22u, Capacitor_SMD:C_0402_1005Metric, F.Cu at (84.3, 72.2)
- added C4: 22u, Capacitor_SMD:C_0402_1005Metric, F.Cu at (84.3, 131.3)
- added C4: 22u, Capacitor_SMD:C_0402_1005Metric, F.Cu at (84.3, 99.8)
- added C4: 22u, Capacitor_SMD:C_0402_1005Metric, F.Cu at (84.3, 68.4)
- added C5: 1u, Capacitor_SMD:C_0402_1005Metric, F.Cu at (84.5, 121.0)
- added C5: 1u, Capacitor_SMD:C_0402_1005Metric, F.Cu at (84.5, 89.6)
- added C5: 1u, Capacitor_SMD:C_0402_1005Metric, F.Cu at (84.5, 58.1)
- added C6: 1u, Capacitor_SMD:C_0402_1005Metric, F.Cu at (84.8, 124.8)
- added C6: 1u, Capacitor_SMD:C_0402_1005Metric, F.Cu at (84.8, 93.4)
- added C6: 1u, Capacitor_SMD:C_0402_1005Metric, F.Cu at (84.8, 61.9)
- added C7: 500n, Capacitor_SMD:C_0402_1005Metric, F.Cu at (84.0, 128.6)
- added C7: 500n, Capacitor_SMD:C_0402_1005Metric, F.Cu at (84.0, 97.2)
- added C7: 500n, Capacitor_SMD:C_0402_1005Metric, F.Cu at (84.0, 65.7)
- added C8: 0.47u, Capacitor_SMD:C_0402_1005Metric, B.Cu at (76.9, 132.5)
- added C8: 0.47u, Capacitor_SMD:C_0402_1005Metric, B.Cu at (76.9, 101.0)
- added C8: 0.47u, Capacitor_SMD:C_0402_1005Metric, B.Cu at (76.9, 69.6)
- added C9: 0.47u, Capacitor_SMD:C_0402_1005Metric, B.Cu at (106.8, 129.5)
- added C9: 0.47u, Capacitor_SMD:C_0402_1005Metric, B.Cu at (106.8, 98.1)
- added C9: 0.47u, Capacitor_SMD:C_0402_1005Metric, B.Cu at (106.8, 66.6)
- added D1: WS2812B, LED_SMD:LED_WS2812B_PLCC4_5.0x5.0mm_P3.2mm, F.Cu at (113.8, 122.5)
- added D1: WS2812B, LED_SMD:LED_WS2812B_PLCC4_5.0x5.0mm_P3.2mm, F.Cu at (113.8, 91.1)
- added D1: WS2812B, LED_SMD:LED_WS2812B_PLCC4_5.0x5.0mm_P3.2mm, F.Cu at (113.8, 59.7)
- added D2: D_Schottky, Diode_SMD:D_0402_1005Metric, F.Cu at (59.4, 126.4)
- added D2: D_Schottky, Diode_SMD:D_0402_1005Metric, F.Cu at (59.4, 94.9)
- added D2: D_Schottky, Diode_SMD:D_0402_1005Metric, F.Cu at (59.4, 63.5)
- added D3: D_Schottky, Diode_SMD:D_0402_1005Metric, B.Cu at (71.0, 132.3)
- added D3: D_Schottky, Diode_SMD:D_0402_1005Metric, B.Cu at (71.0, 100.9)
- added D3: D_Schottky, Diode_SMD:D_0402_1005Metric, B.Cu at (71.0, 69.4)
- added D4: D_Schottky, Diode_SMD:D_0402_1005Metric, F.Cu at (59.4, 128.6)
- added D4: D_Schottky, Diode_SMD:D_0402_1005Metric, F.Cu at (59.4, 97.2)
- added D4: D_Schottky, Diode_SMD:D_0402_1005Metric, F.Cu at (59.4, 65.7)
- added D5: D_Schottky, Diode_SMD:D_0402_1005Metric, B.Cu at (100.3, 134.0)
- added D5: D_Schottky, Diode_SMD:D_0402_1005Metric, B.Cu at (100.3, 102.5)
- added D5: D_Schottky, Diode_SMD:D_0402_1005Metric, B.Cu at (100.3, 71.1)
- added D6: D_Schottky, Diode_SMD:D_0402_1005Metric, B.Cu at (68.0, 131.2)
- added D6: D_Schottky, Diode_SMD:D_0402_1005Metric, B.Cu at (68.0, 99.7)
- added D6: D_Schottky, Diode_SMD:D_0402_1005Metric, B.Cu at (68.0, 68.3)
- added D7: LED, LED_SMD:LED_0402_1005Metric, F.Cu at (58.9, 124.8)
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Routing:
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- added copper zone on F.Cu, net Board_1-GND
- added copper zone on F.Cu, net Board_2-GND
- added copper zone on F.Cu, net Board_3-GND
- removed copper zone on F.Cu, net (none)
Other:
- outline, holes or cut-outs redrawn
